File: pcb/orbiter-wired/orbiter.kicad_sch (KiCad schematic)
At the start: 26 parts, among them U1 TPS82140SILR

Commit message: Latest WIP
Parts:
- removed NRST_TP1, SWCLK_TP1, SWDIO_TP1: TestPoint_Small, Testpoint_Rev:TestPoint_THTPad_D1.0mm_Drill0.5mm_reversible, symbol Connector:TestPoint_Small
- added J1: SWD, Connector_PinSocket_2.54mm:PinSocket_2x05_P2.54mm_Vertical, symbol Connector_Generic:Conn_02x05_Odd_Even
- added J3: I2C Extension, Connector_PinSocket_2.54mm:PinSocket_1x04_P2.54mm_Vertical, symbol Connector_Generic:Conn_01x04
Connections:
- net GND: now also J1.3 (Pin_3), J1.5 (Pin_5), J1.9 (Pin_9), J3.4 (Pin_4)
- net NRST: now also J1.10 (Pin_10)
- net SWCLK: now also J1.4 (Pin_4)
- net SWDIO: now also J1.2 (Pin_2)
- net TPS_VOUT: now also J1.1 (Pin_1), J3.3 (Pin_3)
- net USART renamed USART_TX
- new net I2C2_SCL: J3.2 (Pin_2)
- new net I2C2_SDA: J3.1 (Pin_1)
- no-connect marks 0 -> 3
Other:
- sheet MCU_BOTTOM ports: added I2C2_SCL, I2C2_SDA, LED1, USART3_RX; removed none
- sheet MCU_TOP ports: added I2C2_SCL, I2C2_SDA, LED1, USART3_RX; removed none
- note added: "Debug port (Cortex JTAG mapping)"
- note added: "I2C extension port"
- moved on the sheet: 3V3_TP1, BOOT0_TP1, USART_TP1, USB_CONN_DN_TP1, USB_CONN_DP_TP1, USB_DN_TP1, VBUS_TP1

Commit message: No DRC errors with new clean layout
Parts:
- removed 3V3_TP1, BOOT0_TP1, USART_TP1, USB_CONN_DN_TP1, USB_CONN_DP_TP1, USB_DN_TP1, USB_DP_TP1, VBUS_TP1: TestPoint_Small, Testpoint_Rev:TestPoint_THTPad_D1.0mm_Drill0.5mm_reversible, symbol Connector:TestPoint_Small
- added J5: Keyboard matrix, Connector_PinSocket_2.54mm:PinSocket_1x11_P2.54mm_Vertical, symbol Connector_Generic:Conn_01x11
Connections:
- net T_KEY_COL0: now also J5.1 (Pin_1)
- net T_KEY_COL1: now also J5.2 (Pin_2)
- net T_KEY_COL2: now also J5.3 (Pin_3)
- net T_KEY_COL3: now also J5.4 (Pin_4)
- net T_KEY_COL4: now also J5.5 (Pin_5)
- net T_KEY_COL5: now also J5.6 (Pin_6)
- net T_KEY_ROW0: now also J5.7 (Pin_7)
- net T_KEY_ROW1: now also J5.8 (Pin_8)
- net T_KEY_ROW2: now also J5.9 (Pin_9)
- net T_KEY_ROW3: now also J5.10 (Pin_10)
- net T_KEY_ROW4: now also J5.11 (Pin_11)

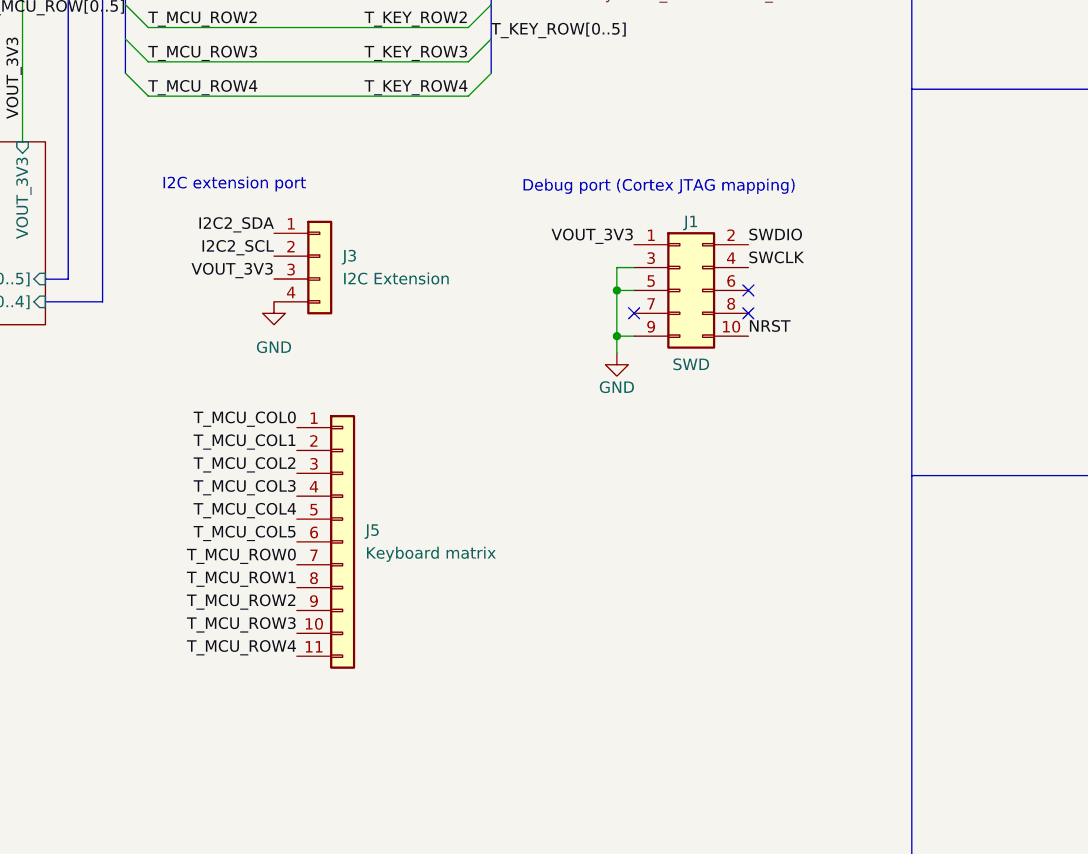
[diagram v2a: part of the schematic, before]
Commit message: Add pull-up for UART RX as well
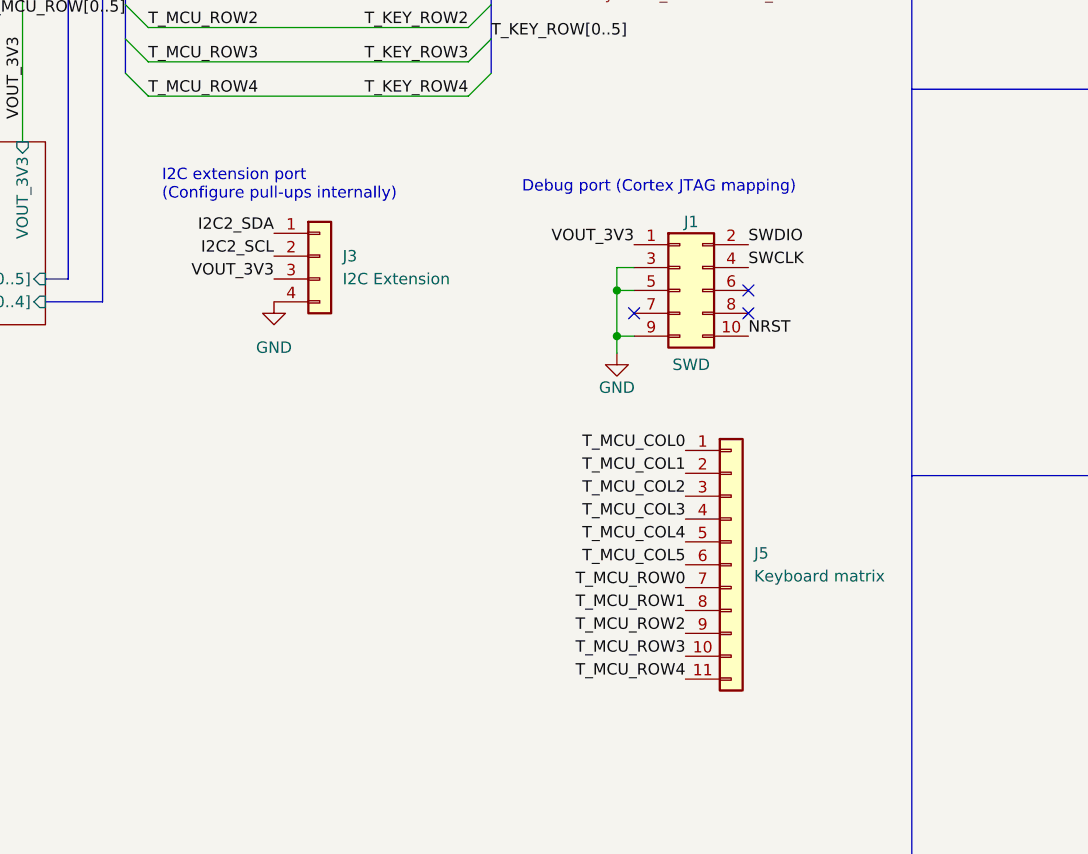
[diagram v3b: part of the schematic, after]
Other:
- note added: "I2C extension port (Configure pull-ups internally)"
- note removed: "I2C extension port"
- moved on the sheet: J5
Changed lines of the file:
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@@
 		)
 	)
-	(text "I2C extension port"
+	(text "I2C extension port\n(Configure pull-ups internally)"
 		(exclude_from_sim no)
 		(at 101.854 83.566 0)
@@
 	)
 	(label "T_MCU_ROW2"
-		(at 116.84 130.81 180)
+		(at 160.02 133.35 180)
 		(fields_autoplaced yes)
 		(effects
@@
 	)
 	(label "T_MCU_COL2"
-		(at 116.84 115.57 180)
+		(at 160.02 118.11 180)
 		(fields_autoplaced yes)
 		(effects
@@
 	)
 	(label "T_MCU_COL1"
-		(at 116.84 113.03 180)
+		(at 160.02 115.57 180)
 		(fields_autoplaced yes)
 		(effects
@@
 	)
 	(label "T_MCU_COL5"
-		(at 116.84 123.19 180)
+		(at 160.02 125.73 180)
 		(fields_autoplaced yes)
 		(effects
@@
 	)
 	(label "T_MCU_ROW3"
-		(at 116.84 133.35 180)
+		(at 160.02 135.89 180)
 		(fields_autoplaced yes)
 		(effects
@@
 	)
 	(label "T_MCU_ROW1"
-		(at 116.84 128.27 180)
+		(at 160.02 130.81 180)
 		(fields_autoplaced yes)
 		(effects
@@
 	)
 	(label "T_MCU_ROW0"
-		(at 116.84 125.73 180)
+		(at 160.02 128.27 180)
 		(fields_autoplaced yes)
 		(effects
@@
 	)
 	(label "T_MCU_COL0"
-		(at 116.84 110.49 180)
+		(at 160.02 113.03 180)
 		(fields_autoplaced yes)
 		(effects
@@
 	)
 	(label "T_MCU_COL4"
-		(at 116.84 120.65 180)
+		(at 160.02 123.19 180)
 		(fields_autoplaced yes)
 		(effects
@@
 	)
 	(label "T_MCU_ROW4"
-		(at 116.84 135.89 180)
+		(at 160.02 138.43 180)
 		(fields_autoplaced yes)
 		(effects
@@
 	)
 	(label "T_MCU_COL3"
-		(at 116.84 118.11 180)
+		(at 160.02 120.65 180)
 		(fields_autoplaced yes)
 		(effects
@@
 	(symbol
 		(lib_id "Connector_Generic:Conn_01x11")
-		(at 121.92 123.19 0)
+		(at 165.1 125.73 0)
 		(unit 1)
 		(exclude_from_sim no)
@@
 		(fields_autoplaced yes)
 		(property "Reference" "J5"
-			(at 124.46 121.9199 0)
+			(at 167.64 124.4599 0)
 			(effects
 				(font
@@
 		)
 		(property "Value" "Keyboard matrix"
-			(at 124.46 124.4599 0)
+			(at 167.64 126.9999 0)
 			(effects
 				(font
@@
 		)
 		(property "Footprint" "Connector_PinSocket_2.54mm:PinSocket_1x11_P2.54mm_Vertical"
-			(at 121.92 123.19 0)
+			(at 165.1 125.73 0)
 			(effects
 				(font
@@
 		)
 		(property "Datasheet" "~"
-			(at 121.92 123.19 0)
+			(at 165.1 125.73 0)
 			(effects
 				(font
@@
 		)
 		(property "Description" "Generic connector, single row, 01x11, script generated (kicad-library-utils/schlib/autogen/connector/)"
-			(at 121.92 123.19 0)
-			(effects
-				(font
+			(at 165.1 125.73 0)
+			(effects
+				(font

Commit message: Add TODOs for fixes for next version
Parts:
- added U2: USBLC6-2P6, Package_TO_SOT_SMD:SOT-666, symbol Power_Protection:USBLC6-2P6
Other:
- note added: "TODO FIX"
- moved on the sheet: C1, C2, H1, H2, H3, H4, H5, H6, H7, J1, J3, J5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
